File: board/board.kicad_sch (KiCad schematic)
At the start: 36 parts, among them J1 ANT, J2 DEBUG, J3 GPIO, P1 USB_C_Plug_USB2.0, SW1 BOOTSEL, SW2 RUN, U1 RP2040, U2 W25Q128JVS, U3 NCP1117-3.3_SOT223, U4 RFM95W-915S2, U5 BLE5201, Y1 ABM8G-12.000MHZ-18-D2Y-T

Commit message: board v2 hour 2
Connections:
- net PC00: no longer names the net of U5.11 (PC00)
- net PC00: no longer J3.9 (Pin_9)
- net PC01: no longer names the net of U5.12 (PC01)
- net PC01: no longer J3.10 (Pin_10)
- net PC02: no longer names the net of U5.13 (PC02)
- net PC02: no longer J3.11 (Pin_11)
- net PC03: no longer names the net of U5.14 (PC03)
- net PC03: no longer J3.12 (Pin_12)
- no-connect marks 6 -> 14
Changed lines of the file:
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@@
+	)
+	(no_connect
+		(at 121.92 135.89)
+	)
+	(no_connect
+		(at 185.42 124.46)
 	)
 	(no_connect
@@
 	)
 	(no_connect
+		(at 185.42 121.92)
+	)
+	(no_connect
 		(at 115.57 102.87)
+	)
+	(no_connect
+		(at 121.92 128.27)
+	)
+	(no_connect
+		(at 185.42 129.54)
+	)
+	(no_connect
+		(at 121.92 133.35)
 	)
 	(no_connect
@@
 	)
 	(no_connect
+		(at 185.42 127)
+	)
+	(no_connect
 		(at 185.42 116.84)
 	)
+	(no_connect
+		(at 121.92 130.81)
+	)
 	(wire
 		(pts
@@
 	(wire
 		(pts
-			(xy 191.77 124.46) (xy 185.42 124.46)
-		)
-		(stroke
-			(width 0)
-			(type default)
-		)
-	)
-	(wire
-		(pts
 			(xy 64.77 128.27) (xy 60.96 128.27)
 		)
@@
 	(wire
 		(pts
-			(xy 191.77 127) (xy 185.42 127)
-		)
-		(stroke
-			(width 0)
-			(type default)
-		)
-	)
-	(wire
-		(pts
 			(xy 115.57 80.01) (xy 144.78 80.01)
 		)
@@
 	(wire
 		(pts
-			(xy 115.57 129.54) (xy 121.92 129.54)
-		)
-		(stroke
-			(width 0)
-			(type default)
-		)
-	)
-	(wire
-		(pts
 			(xy 41.91 121.92) (xy 41.91 124.46)
 		)
@@
 	(wire
 		(pts
-			(xy 115.57 137.16) (xy 121.92 137.16)
-		)
-		(stroke
-			(width 0)
-			(type default)
-		)
-	)
-	(wire
-		(pts
 			(xy 48.26 45.72) (xy 50.8 45.72)
 		)
@@
 	(wire
 		(pts
-			(xy 121.92 128.27) (xy 121.92 129.54)
-		)
-		(stroke
-			(width 0)
-			(type default)
-		)
-	)
-	(wire
-		(pts
 			(xy 41.91 116.84) (xy 49.53 116.84)
 		)
@@
 	(wire
 		(pts
-			(xy 191.77 121.92) (xy 185.42 121.92)
-		)
-		(stroke
-			(width 0)
-			(type default)
-		)
-	)
-	(wire
-		(pts
 			(xy 163.83 74.93) (xy 175.26 74.93)
 		)
@@
 	(wire
 		(pts
-			(xy 191.77 129.54) (xy 185.42 129.54)
-		)
-		(stroke
-			(width 0)
-			(type default)
-		)
-	)
-	(wire
-		(pts
 			(xy 41.91 38.1) (xy 41.91 40.64)
 		)
@@
 	(wire
 		(pts
-			(xy 121.92 137.16) (xy 121.92 135.89)
-		)
-		(stroke
-			(width 0)
-			(type default)
-		)
-	)
-	(wire
-		(pts
 			(xy 60.96 80.01) (xy 64.77 80.01)
 		)
@@
 	(wire
 		(pts
-			(xy 121.92 132.08) (xy 121.92 130.81)
-		)
-		(stroke
-			(width 0)
-			(type default)
-		)
-	)
-	(wire
-		(pts
 			(xy 163.83 62.23) (xy 175.26 62.23)
 		)
@@
 	(wire
 		(pts
-			(xy 115.57 134.62) (xy 121.92 134.62)
-		)
-		(stroke
-			(width 0)
-			(type default)
-		)
-	)
-	(wire
-		(pts
 			(xy 92.71 29.21) (xy 92.71 44.45)
 		)
@@
 	(wire
 		(pts
-			(xy 121.92 134.62) (xy 121.92 133.35)
-		)
-		(stroke
-			(width 0)
-			(type default)
-		)
-	)
-	(wire
-		(pts
 			(xy 21.59 135.89) (xy 31.75 135.89)
 		)
@@
 		(pts
 			(xy 15.24 147.32) (xy 15.24 146.05)
-		)
-		(stroke
-			(width 0)
-			(type default)
-		)
-	)
-	(wire
-		(pts
-			(xy 115.57 132.08) (xy 121.92 132.08)
 		)
 		(stroke
@@
 		)
 	)
-	(label "PC00"
-		(at 191.77 129.54 180)
-		(fields_autoplaced yes)
-		(effects
-			(font
-				(size 1.27 1.27)
-			)
-			(justify right bottom)
-		)
-	)
 	(label "BLE_SWDIO"
 		(at 48.26 151.13 0)
@@
 		)
 	)
-	(label "PC02"
-		(at 191.77 124.46 180)
-		(fields_autoplaced yes)
-		(effects
-			(font
-				(size 1.27 1.27)
-			)
-			(justify right bottom)
-		)
-	)
 	(label "DIO4"
 		(at 175.26 64.77 0)
@@
 		)
 	)
-	(label "PC02"
-		(at 115.57 134.62 0)
-		(fields_autoplaced yes)
-		(effects
-			(font
-				(size 1.27 1.27)
-			)
-			(justify left bottom)
-		)
-	)
-	(label "PC01"
-		(at 191.77 127 180)
-		(fields_autoplaced yes)
-		(effects
-			(font
-				(size 1.27 1.27)
-			)
-			(justify right bottom)
-		)
-	)
 	(label "DIO5"
 		(at 175.26 62.23 0)
@@
 		)
 	)
-	(label "PC03"
-		(at 115.57 137.16 0)
-		(fields_autoplaced yes)
-		(effects
-			(font
-				(size 1.27 1.27)
-			)
-			(justify left bottom)
-		)
-	)
 	(label "DIO1"
 		(at 175.26 72.39 0)
@@
 		)
 	)
-	(label "PC01"
-		(at 115.57 132.08 0)
-		(fields_autoplaced yes)
-		(effects
-			(font
-				(size 1.27 1.27)
-			)
-			(justify left bottom)
-		)
-	)
 	(label "DIO1"
 		(at 118.11 64.77 0)
@@
 		)
 	)
-	(label "PC00"
-		(at 115.57 129.54 0)
-		(fields_autoplaced yes)
-		(effects
-			(font
-				(size 1.27 1.27)
-			)
-			(justify left bottom)
-		)
-	)
-	(label "PC03"
-		(at 191.77 121.92 180)
-		(fields_autoplaced yes)
-		(effects
-			(font
-				(size 1.27 1.27)
-			)
-			(justify right bottom)
-		)
-	)

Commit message: finish board v2
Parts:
- removed P1: USB_C_Plug_USB2.0, Connector_USB:USB_C_Receptacle_G-Switch_GT-USB-7010ASV, symbol Connector:USB_C_Receptacle_USB2.0_14P
- removed R3, R4: 5.1k, Resistor_SMD:R_0402_1005Metric, symbol Device:R_Small
- added J4: USB_B_Micro, Connector_USB:USB_Micro-B_Amphenol_10118194_Horizontal, symbol Connector:USB_B_Micro
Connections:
- net GND: now also J4.5 (GND), J4.6 (Shield)
- net VBUS: now also J4.1 (VBUS)
- net at R2.1: now also J4.3 (D+)
- net at R1.1: now also J4.2 (D-)
- no-connect marks 14 -> 15

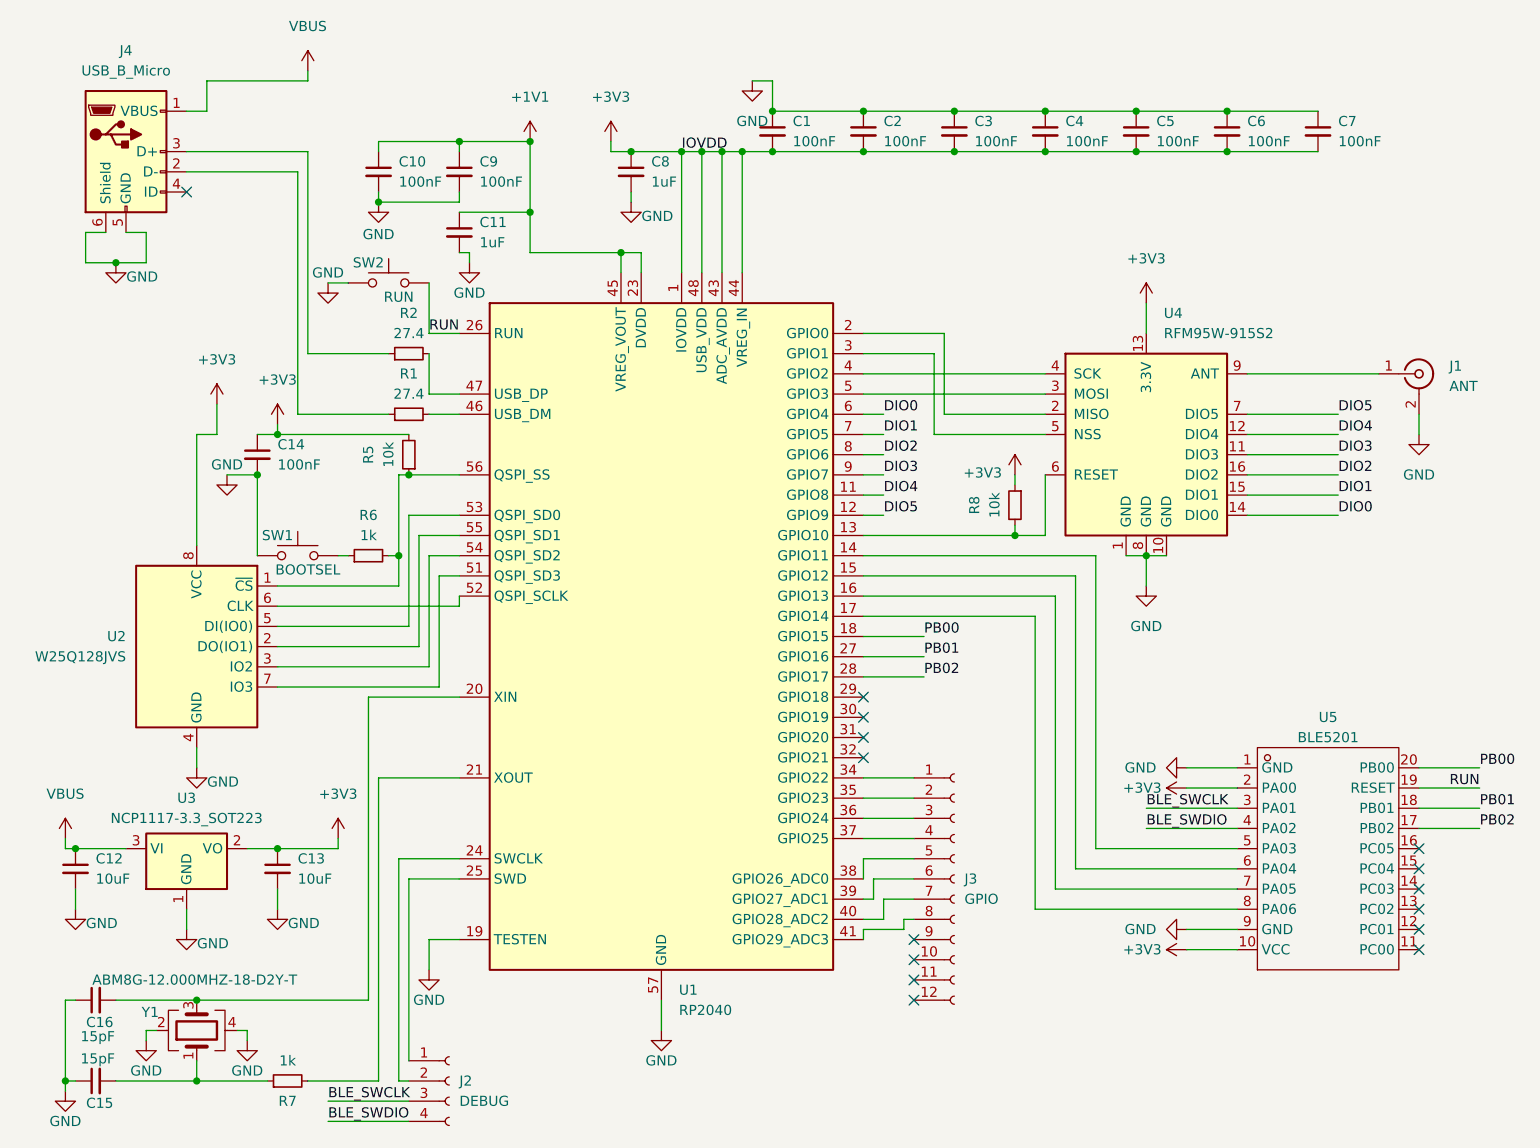
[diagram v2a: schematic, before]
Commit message: appease jlcpcb (component swaps)
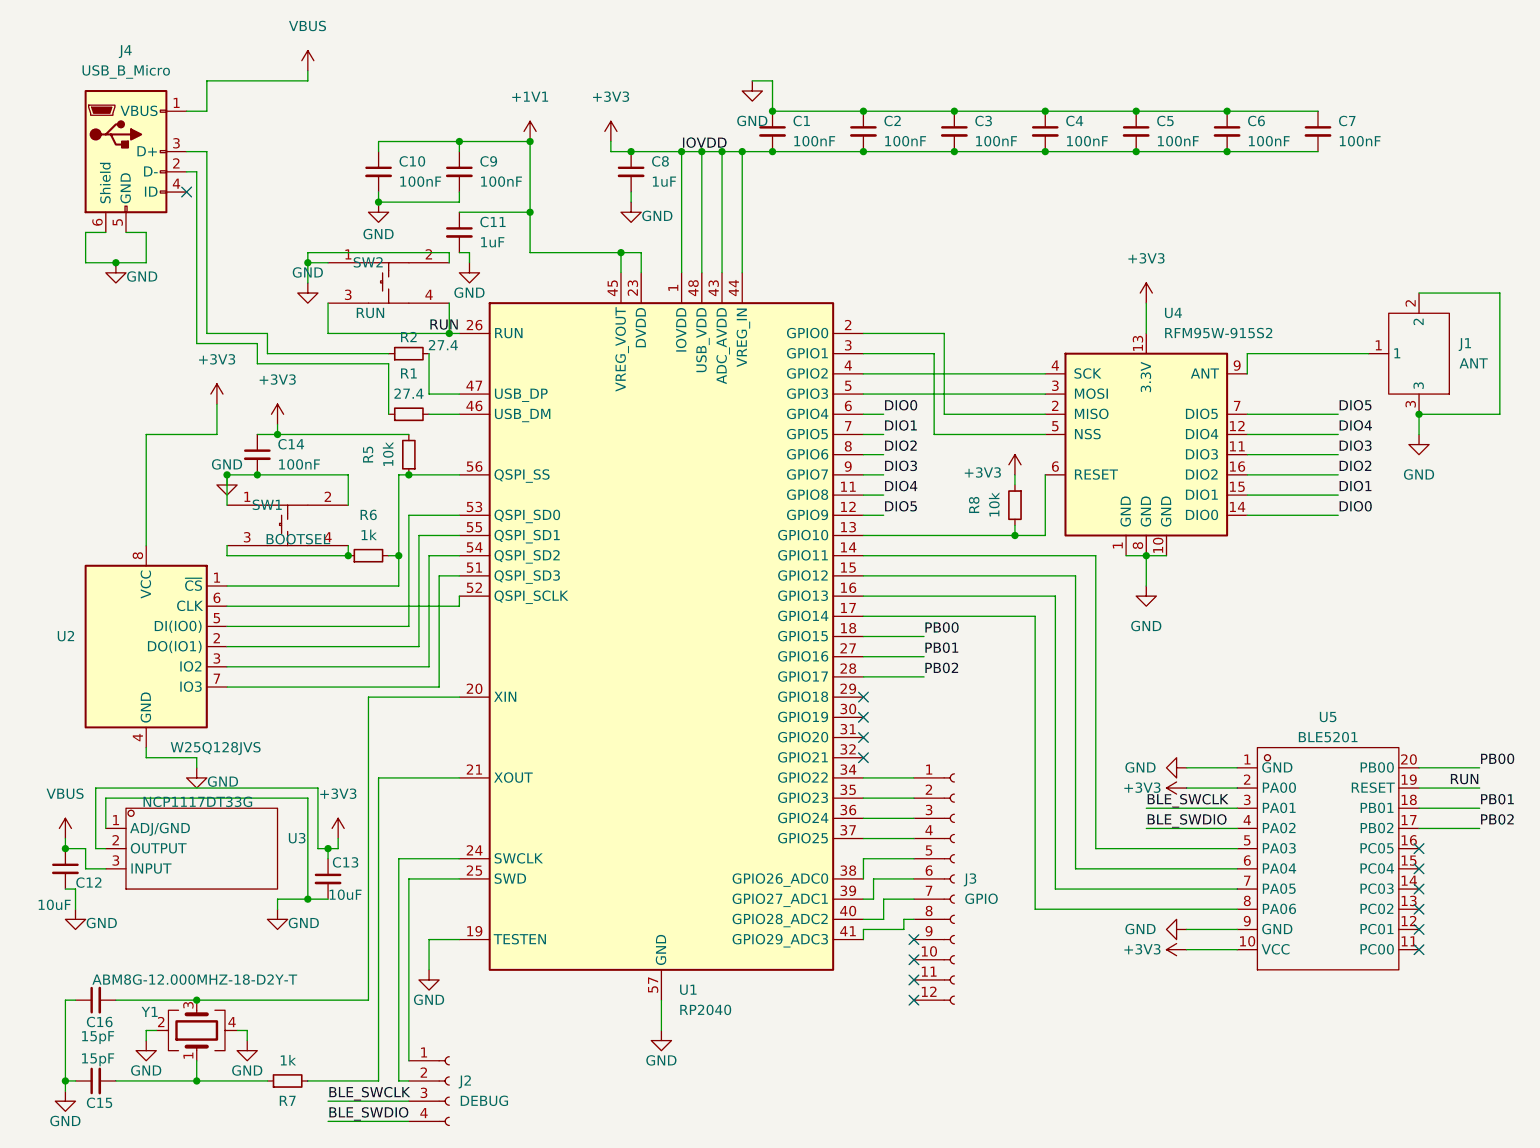
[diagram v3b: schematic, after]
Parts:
- J1: footprint Connector_Coaxial:U.FL_Hirose_U.FL-R-SMT-1_Vertical -> BWU.FL-IPEX1:BWU.FL-IPEX1; symbol Connector:Conn_Coaxial -> BWU.FL-IPEX1:BWU.FL-IPEX1; LCSC Part Name (none) -> 内针 IPEX; Manufacturer (none) -> BAT WIRELESS(蝙蝠无线); Manufacturer Part (none) -> BWU.FL-IPEX1; Supplier (none) -> LCSC; Supplier Part (none) -> C5137195
- SW1, SW2: footprint Button_Switch_SMD:SW_Push_SPST_NO_Alps_SKRK -> K2-1102DP-L3SW-04:SW-TH_4P-L6.0-W6.0-P4.50-LS6.5; symbol Switch:SW_Push -> K2-1102DP-L3SW-04:K2-1102DP-L3SW-04; LCSC Part Name (none) -> K2-1102DP-L3SW-04; Manufacturer (none) -> 韩国韩荣; Manufacturer Part (none) -> K2-1102DP-L3SW-04; Supplier (none) -> LCSC; Supplier Part (none) -> C445493
- U3: value NCP1117-3.3_SOT223 -> NCP1117DT33G; footprint Package_TO_SOT_SMD:SOT-223-3_TabPin2 -> NCP1117DT50G:NCP1117DT50G; symbol Regulator_Linear:NCP1117-3.3_SOT223 -> NCP1117DT50G:NCP1117DT50G; LCSC Part Name (none) -> 输入20V 输出5V 1A; Manufacturer (none) -> onsemi(安森美); Manufacturer Part (none) -> NCP1117DT50G; Supplier (none) -> LCSC; Supplier Part (none) -> C232664
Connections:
- net GND: now also J1.3, SW1.2, SW2.2
- net RUN: now also SW2.3, SW2.4; no longer SW2.2
- net at R6.1: now also SW1.3, SW1.4; no longer SW1.2
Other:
- moved on the sheet: C12, C13, U2, U3
